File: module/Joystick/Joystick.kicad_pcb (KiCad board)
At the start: 2 copper layers, 40 x 32 mm, 14 parts, among them J1 Right Arm, J2 Right Leg, J3 Header 1, J4 Left Arm, J5 Header 1, U1 COM-09032, U7 24AA02-OT, U9 ADS1115IDGS

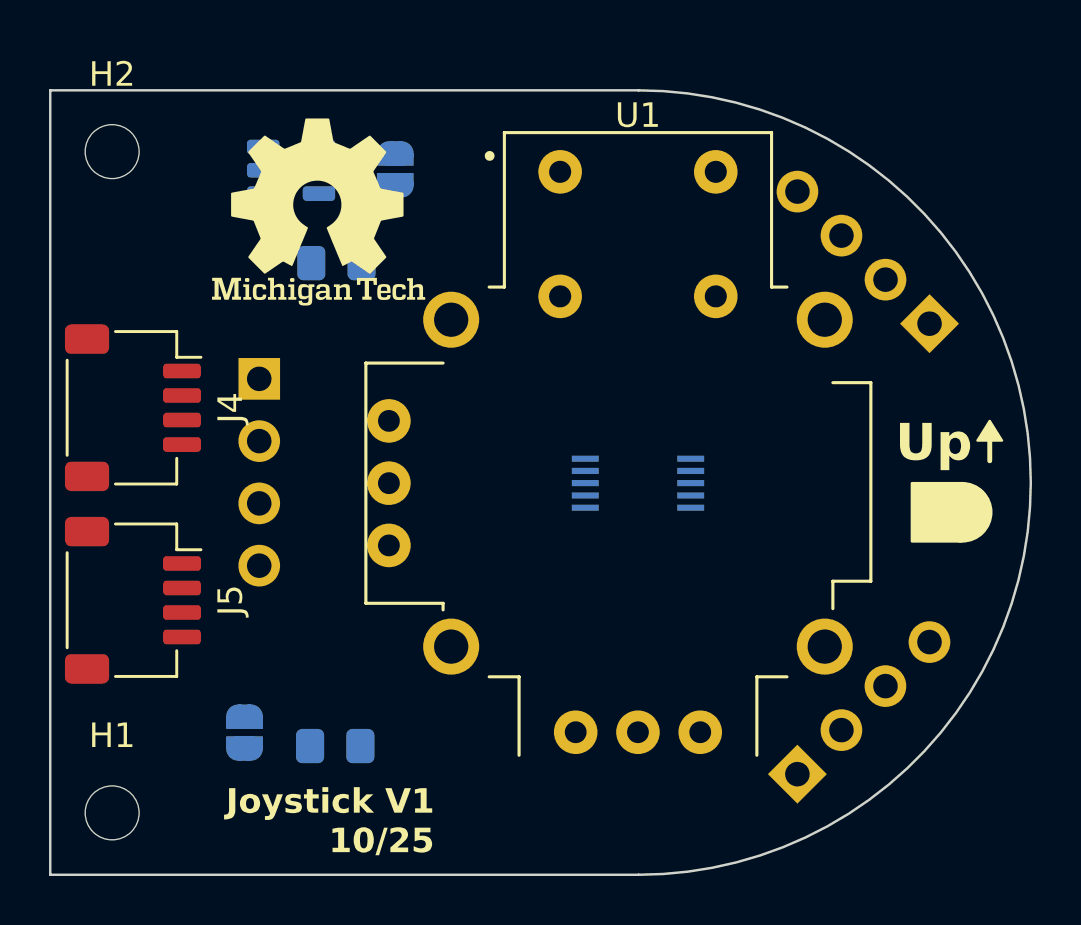
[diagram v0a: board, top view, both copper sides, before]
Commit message: updated templet and renamed lib files
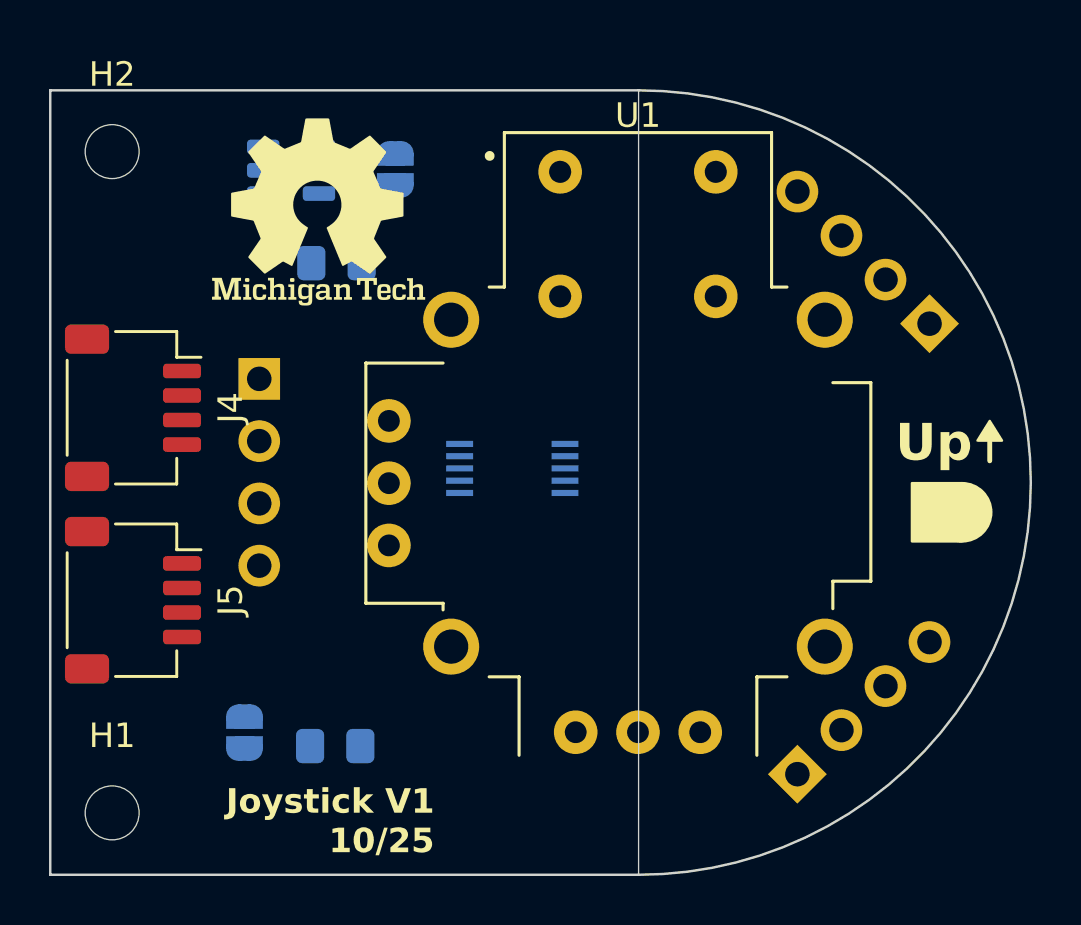
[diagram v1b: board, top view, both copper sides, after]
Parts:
- moved U9 5.16 mm to (84.5, 103.9)
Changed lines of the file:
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@@
 	(footprint "Package_SO:TSSOP-10_3x3mm_P0.5mm"
 		(layer "B.Cu")
-		(at 89.675 104.5)
+		(at 84.55 103.9)
 		(descr "TSSOP10: plastic thin shrink small outline package; 10 leads; body width 3 mm; (see NXP SSOP-TSSOP-VSO-REFLOW.pdf and sot552-1_po.pdf)")
 		(tags "SSOP 0.5")
@@
 		(layer "Edge.Cuts")
 	)
+	(gr_line
+		(start 89.7 120.475)
+		(end 89.7 88.475)
+		(stroke
+			(width 0.05)
+			(type default)
+		)
+		(layer "Edge.Cuts")
+	)
 	(image
 		(at 196.3 96.907159)
@@
 				)
 			)
+		)
+	)
+	(dimension
+		(type orthogonal)
+		(layer "Edge.Cuts")
+		(pts
+			(xy 89.7 104.475) (xy 98.875 95.3)
+		)
+		(height -19.05)
+		(orientation 0)
+		(format
+			(prefix "")
+			(suffix "")
+			(units 3)
+			(units_format 0)
+			(precision 4)
+			(suppress_zeroes yes)
+		)
+		(style
+			(thickness 0.05)
+			(arrow_length 1.27)
+			(text_position_mode 0)
+			(arrow_direction outward)
+			(extension_height 0.58642)
+			(extension_offset 0.5)
+			(keep_text_aligned yes)
+		)
+		(gr_text "9.175"
+			(at 94.2875 84.275 0)
+			(layer "Edge.Cuts")
+			(effects
+				(font
+					(size 1 1)
+					(thickness 0.15)
+				)
+			)
+		)
+	)
+	(dimension
+		(type orthogonal)
+		(layer "Edge.Cuts")
+		(pts
+			(xy 98.875 95.3) (xy 89.7 104.475)
+		)
+		(height 9.125)
+		(orientation 1)
+		(format
+			(prefix "")
+			(suffix "")
+			(units 3)
+			(units_format 0)
+			(precision 4)
+			(suppress_zeroes yes)
+		)
+		(style
+			(thickness 0.05)
+			(arrow_length 1.27)
+			(text_position_mode 0)
+			(arrow_direction outward)
+			(extension_height 0.58642)
+			(extension_offset 0.5)
+			(keep_text_aligned yes)
+		)
+		(gr_text "9.175"
+			(at 106.85 99.8875 90)
+			(layer "Edge.Cuts")
+			(effects
+				(font
+					(size 1 1)
+					(thickness 0.15)
+				)
+			)
